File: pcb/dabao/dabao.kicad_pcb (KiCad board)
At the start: 2 copper layers, 130.8 x 89.3 mm, 69 parts, among them J1 Conn_01x05, J2 USB_C_Receptacle_USB2.0_16P, J3 Conn_01x04, J4 MagConn_01x04_Pin, J5 Conn_Battery, J6 Conn_01x04, J7 Conn_01x04, J8 Display, SW1 SW_RESET, SW2 SW_POWER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

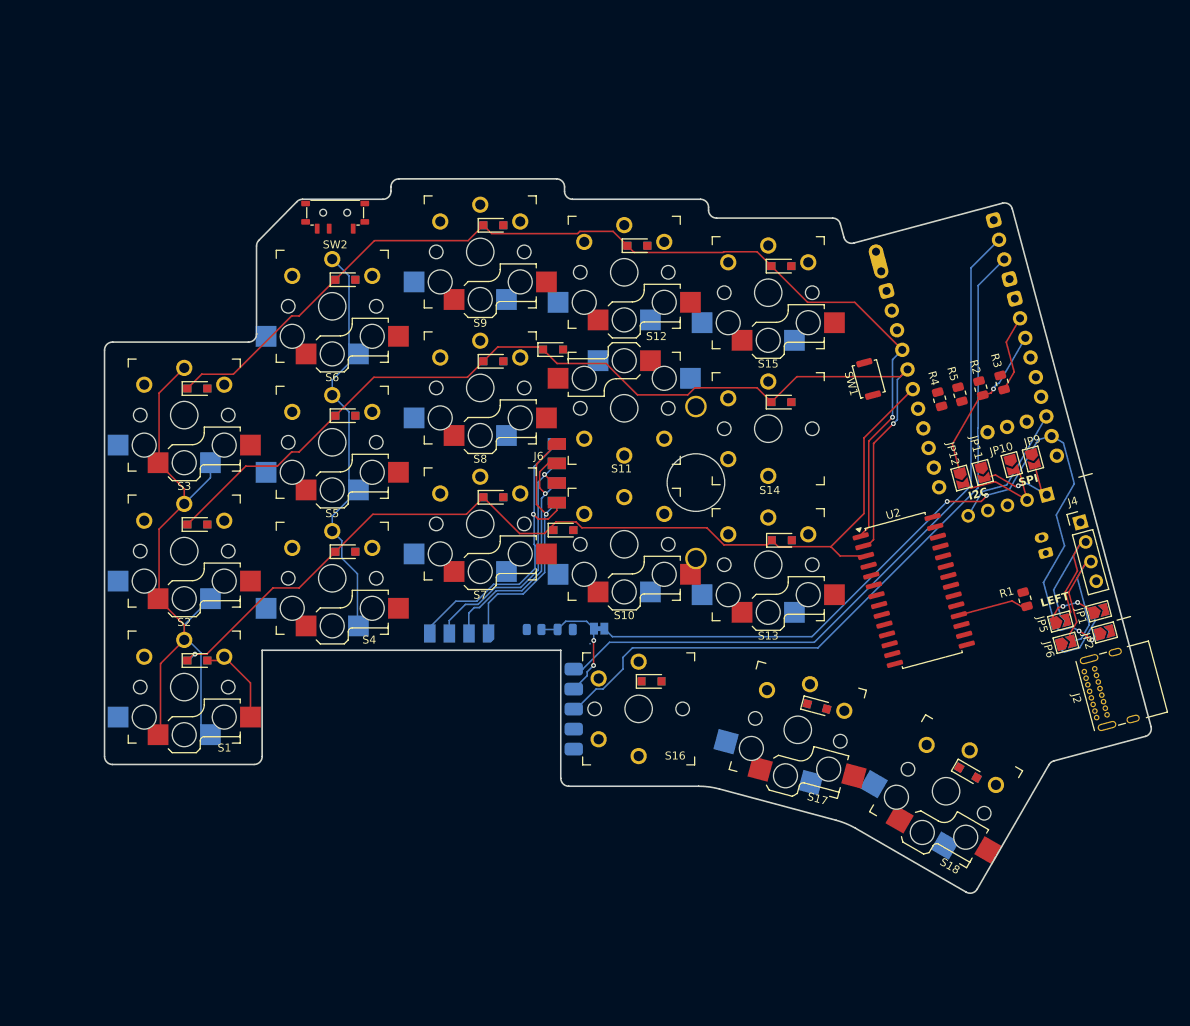
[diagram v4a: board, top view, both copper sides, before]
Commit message: Move trackpoint to thumb, routing
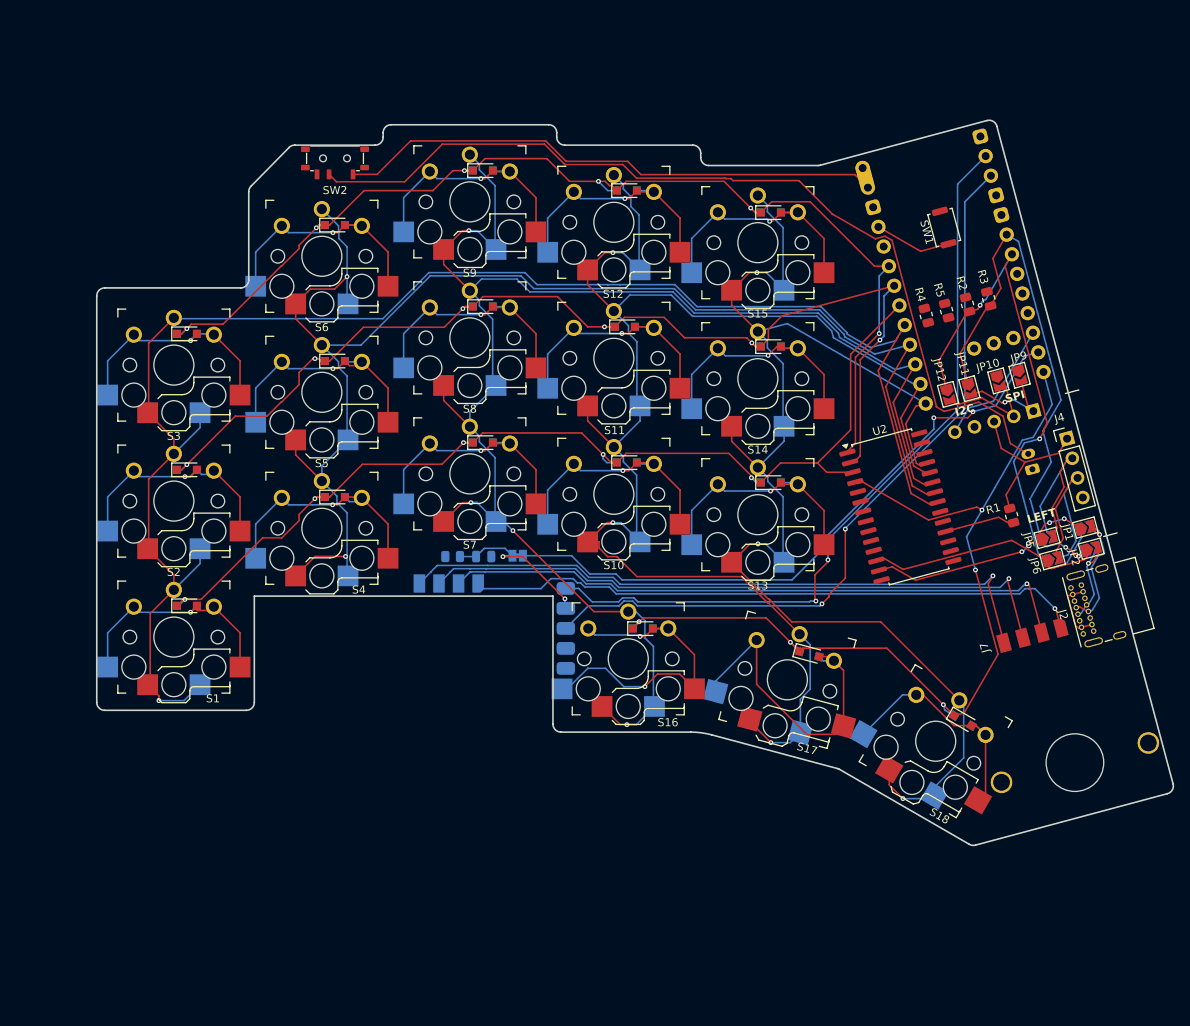
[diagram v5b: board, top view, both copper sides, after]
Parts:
- removed J6: Conn_01x04, Library:TPSensorModule_Connector
- J7: moved to F.Cu
- S14, S16: footprint Library:SW_PG1350_reversible -> Library:Kailh_socket_PG1350_optional_reversible.kicad_mod
- moved J7 62.8 mm to (209.1, 128.9), turned to -75 degrees
- moved REF** 58.9 mm to (214.4, 144.8), turned to 105 degrees
- moved SW1 21.1 mm to (198.0, 78.0)
- moved JP13 13.7 mm to (144.7, 119.0)
- moved R8 13.7 mm to (136.6, 119.1)
- moved C1 13.7 mm to (140.5, 119.1)
- moved D10 11.6 mm to (158.4, 107.3)
- moved J4 10.6 mm to (213.4, 104.3)
- moved JP11 10.6 mm to (201.2, 98.1)
- moved JP2 10.6 mm to (216.4, 118.1)
- moved U1 10.6 mm to (199.5, 84.5)
- moved JP6 10.6 mm to (211.6, 119.4)
- moved JP8 10.6 mm to (211.6, 119.4)
- moved JP7 10.6 mm to (210.8, 116.8)
- moved U2 10.6 mm to (192.6, 112.9)
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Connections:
- U1 pad 20: /col_inner -> /col_pinky
- U1 pad 21: /col_index -> /col_ring
- U1 pad 23: /col_ring -> /col_index
- U1 pad 24: /col_pinky -> /col_inner
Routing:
- net /col_middle: track 0.00 -> 198.1 mm, vias 0 -> 4
- net /col_index: track 0.00 -> 186.0 mm, vias 0 -> 3
- net /col_inner: track 0.00 -> 167.9 mm, vias 0 -> 3
- net /col_ring: track 52.6 -> 180.7 mm, vias 0 -> 2
- net /col_pinky: track 79.1 -> 199.1 mm, vias 0 -> 1
- net /row_thumb: track 0.00 -> 117.7 mm, vias 0 -> 5
- net Net-(J5-Pin_2): track 0.00 -> 114.3 mm
- net /BAT+: track 0.00 -> 68.5 mm
- net Net-(J3-Pin_3): track 30.9 -> 81.1 mm
- net Net-(J3-Pin_2): track 30.5 -> 79.4 mm
- net Net-(J3-Pin_1): track 31.4 -> 77.5 mm
- net Net-(J3-Pin_4): track 38.4 -> 82.8 mm
- net /SCL_Right: track 28.3 -> 70.6 mm, vias 1 -> 2
- net Net-(D16-A): track 0.00 -> 41.6 mm, vias 0 -> 2
- net Net-(D17-A): track 0.00 -> 40.8 mm
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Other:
- board size 130.8 x 89.3 mm -> 134.6 x 90.6 mm

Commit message: Finish routing
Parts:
- moved S1 18.5 mm to (98.4, 110.9), turned to -15 degrees
- moved S3 17.9 mm to (107.2, 78.1), turned to -15 degrees
- moved D1 17.8 mm to (101.0, 107.6), turned to -15 degrees
- moved D3 17.7 mm to (109.8, 74.7), turned to -15 degrees
- moved S2 17.7 mm to (102.8, 94.5), turned to -15 degrees
- moved D2 17.2 mm to (105.4, 91.1), turned to -15 degrees
- moved SW2 15.9 mm to (133.3, 58.3), turned to -15 degrees
- moved REF** 15.3 mm to (203.1, 155.2), turned to 90 degrees
- moved D6 14.6 mm to (131.2, 66.4), turned to -15 degrees
- moved S6 14.5 mm to (128.6, 69.7), turned to -15 degrees
- moved J2 13.3 mm to (208.3, 140.0), turned to 90 degrees
- moved S5 13.0 mm to (124.2, 86.1), turned to -15 degrees
- moved S4 13.0 mm to (119.8, 102.6), turned to -15 degrees
- moved D5 12.8 mm to (126.8, 82.8), turned to -15 degrees
- moved JP2 12.6 mm to (212.0, 129.9), turned to 0 degrees
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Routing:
- net VDD: track 27.8 -> 196.4 mm, vias 0 -> 8
- net GND: track 0.00 -> 67.0 mm, vias 0 -> 68
- net /SCK: track 0.00 -> 14.0 mm, vias 0 -> 1
- net /MOSI: track 0.00 -> 7.96 mm, vias 0 -> 1
- net /PS2_CLK: track 96.1 -> 103.7 mm, vias 2 -> 3
- net /row_top: track 139.4 -> 141.3 mm
- net /PS2_Data: track 96.9 -> 98.6 mm, vias 2 -> 3
- net Net-(J1-Pin_2): track 19.8 -> 21.1 mm
- net /TP_reset: track 80.0 -> 78.9 mm
- net /col_middle: track 198.1 -> 198.7 mm
- net Net-(D16-A): track 41.6 -> 41.1 mm
- added copper zone on B.Cu, net GND
- added copper zone on F.Cu, net GND
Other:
- board size 134.6 x 90.6 mm -> 127.4 x 106.6 mm

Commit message: Update routing
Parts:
- added REF**: MountingHole_2.2mm_M2, MountingHole:MountingHole_2.2mm_M2, F.Cu at (162.9, 125.1)
- added REF**: MountingHole_2.2mm_M2, MountingHole:MountingHole_2.2mm_M2, F.Cu at (138.8, 60.6)
- added REF**: MountingHole_2.2mm_M2, MountingHole:MountingHole_2.2mm_M2, F.Cu at (129.9, 106.4)
- added REF**: MountingHole_2.2mm_M2, MountingHole:MountingHole_2.2mm_M2, F.Cu at (170.0, 84.3)
- added REF**: MountingHole_2.2mm_M2, MountingHole:MountingHole_2.2mm_M2, F.Cu at (112.4, 88.5)
- added REF**: MountingHole_2.2mm_M2, MountingHole:MountingHole_2.2mm_M2, F.Cu at (190.2, 132.6)
- moved REF** 5.02 mm to (201.8, 160.1)
- moved JP10 2.32 mm to (205.3, 104.5)
- moved D18 2.32 mm to (190.0, 144.4)
- moved JP4 2.32 mm to (211.0, 127.8)
- moved JP9 2.32 mm to (208.1, 104.5)
- moved SW1 2.32 mm to (203.7, 84.3)
- moved R5 2.32 mm to (201.3, 94.4)
- moved J2 2.32 mm to (207.4, 137.8)
- moved J7 2.32 mm to (201.2, 136.3)
- moved C1 2.32 mm to (137.5, 109.1)
- moved D14 2.32 mm to (179.0, 93.0)
- moved D2 2.32 mm to (104.5, 89.0)
- moved D5 2.32 mm to (125.8, 80.7)
- moved D6 2.32 mm to (130.2, 64.2)
- moved J5 2.32 mm to (206.6, 116.3)
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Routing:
- net /col_index: track 186.0 -> 184.5 mm
- net /row_thumb: track 117.7 -> 119.0 mm
- net Net-(J5-Pin_2): track 114.4 -> 115.1 mm
- net /row_top: track 141.3 -> 141.8 mm

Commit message: Update pcb outline, final-ish drc checks
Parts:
- moved J7 2.84 mm to (201.2, 133.5)
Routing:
- net Net-(J3-Pin_4): track 82.8 -> 80.0 mm
- net Net-(J3-Pin_2): track 79.4 -> 76.6 mm
- net Net-(J3-Pin_3): track 81.1 -> 78.6 mm
- net Net-(J3-Pin_1): track 77.5 -> 75.7 mm
- net /row_top: track 141.8 -> 141.2 mm
- net GND: vias 68 -> 70
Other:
- board size 127.4 x 106.6 mm -> 127.4 x 114.6 mm
- board text added: "打包 v1.0"
